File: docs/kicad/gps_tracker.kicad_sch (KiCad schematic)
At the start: 12 parts, among them J1 GNSS: Foxeer M10Q-250 / Beiti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, J2 BIGGA GSM (SIM800C) board, J3 SSD1306 0.96" OLED I2C 0x3C, J4 MicroSD SPI module, J5 Battery Shield V8, 2x18650, J6 BMA400 CJMCU-400 (not fitted 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, SW1 Button (BOOT-style, active lo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, U1 ESP32-S3-WROOM-1 (DevKitC-1)

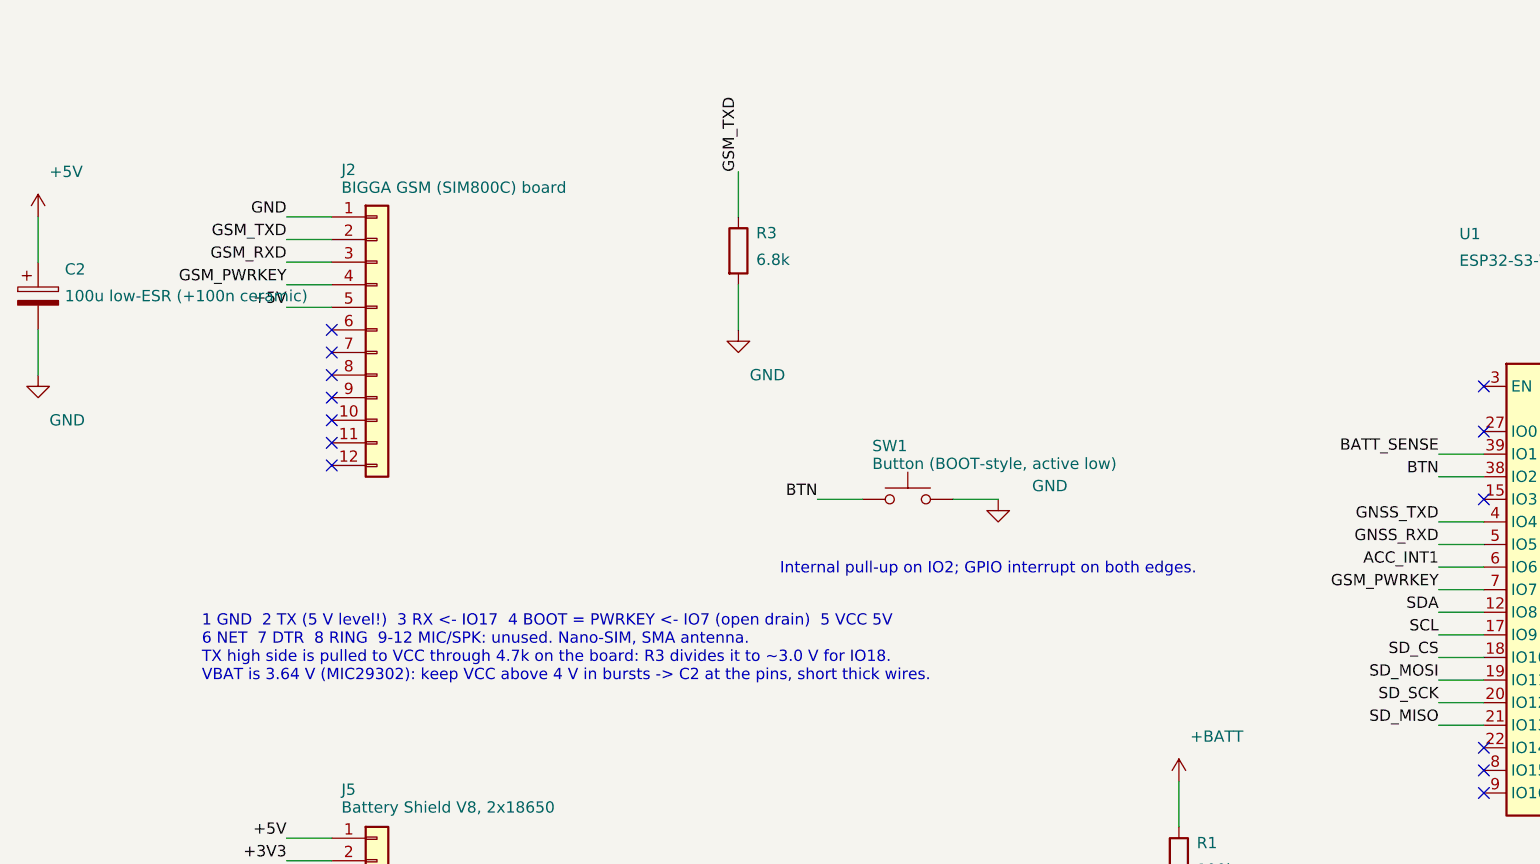
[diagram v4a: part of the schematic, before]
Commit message: Schematic: move C2 clear of the BIGGA header labels
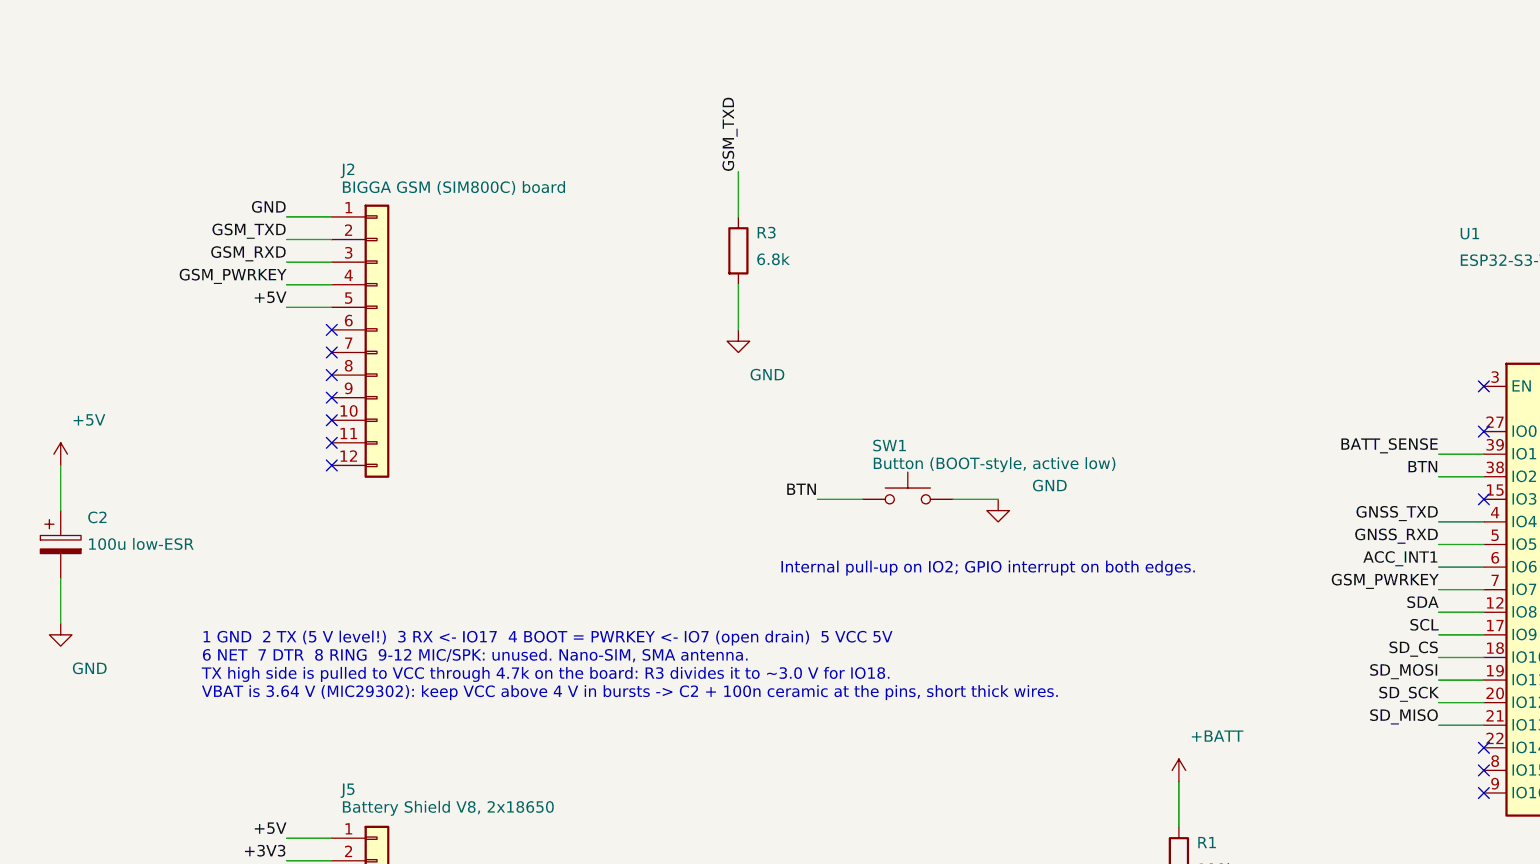
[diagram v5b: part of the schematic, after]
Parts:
- C2: value 100u low-ESR (+100n ceramic) -> 100u low-ESR
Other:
- note added: "1 GND 2 TX (5 V level!) 3 RX <- IO17 4 BOOT = PWRKEY <- IO7 (open drain) 5 VCC 5V 6 NET 7 DTR 8 RING 9-12 MIC/SPK: unused. Nano-SIM, SMA antenna. TX high side is pulled to VCC through 4.7k on the board: R3 divides it to ~3.0 V for IO18. VBAT is 3.64 V (MIC29302): keep VCC above 4 V in bursts -> C2 + 100n ceramic at the pins, short thick wires."
- note removed: "1 GND 2 TX (5 V level!) 3 RX <- IO17 4 BOOT = PWRKEY <- IO7 (open drain) 5 VCC 5V 6 NET 7 DTR 8 RING 9-12 MIC/SPK: unused. Nano-SIM, SMA antenna. TX high side is pulled to VCC through 4.7k on the board: R3 divides it to ~3.0 V for IO18. VBAT is 3.64 V (MIC29302): keep VCC above 4 V in bursts -> C2 at the pins, short thick wires."

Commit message: NET indicator LED on the BIGGA board: 1k + red LED on NETLIGHT
The modem's NETLIGHT output reaches the header as NET; blinking at 0.8 s
means searching, 3 s registered, 0.3 s GPRS transfer. A red LED through
1 k to GND makes that visible on the bench with no firmware involved and
no GPIO spent, which the SuperMini cannot spare. Added to the schematic
(R4, LED1), the hardware doc and the wiring sheet.
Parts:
- added LED1: red NET, symbol Device:LED
- added R4: 1k, symbol Device:R
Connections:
- net GND: now also LED1.1 (K)
- net GSM_NET: now reaches J2.6 (Pin_6)
- net GSM_NET: now also R4.1
- new net: LED1.2 (A), R4.2
- no-connect marks 31 -> 30
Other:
- note added: "1 GND 2 TX (5 V level!) 3 RX <- IO17 4 BOOT = PWRKEY <- IO7 (open drain) 5 VCC 5V 6 NET -> R4 1k -> LED1 (NETLIGHT: 0.8 s searching, 3 s registered, 0.3 s GPRS) 7 DTR 8 RING 9-12 audio: unused. TX high side is pulled to VCC through 4.7k on the board: R3 divides it to ~3.0 V for IO18. VBAT is 3.64 V (MIC29302): keep VCC above 4 V in bursts -> C2 + 100n ceramic at the pins, short thick wires."
- note removed: "1 GND 2 TX (5 V level!) 3 RX <- IO17 4 BOOT = PWRKEY <- IO7 (open drain) 5 VCC 5V 6 NET 7 DTR 8 RING 9-12 MIC/SPK: unused. Nano-SIM, SMA antenna. TX high side is pulled to VCC through 4.7k on the board: R3 divides it to ~3.0 V for IO18. VBAT is 3.64 V (MIC29302): keep VCC above 4 V in bursts -> C2 + 100n ceramic at the pins, short thick wires."

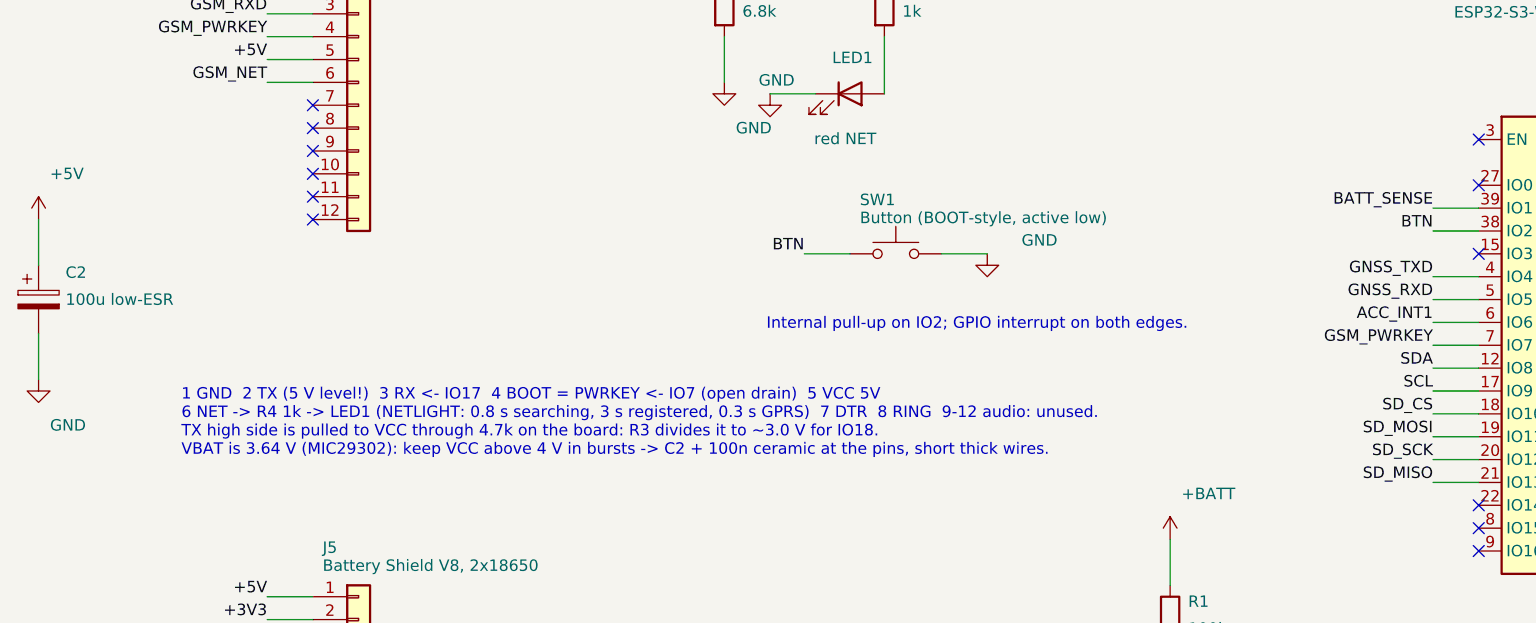
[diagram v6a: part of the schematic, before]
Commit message: BIGGA GSM: no external input capacitor, the board carries 100+10+1 uF at VCC
The board schematic shows C6/C5/C8 (100 uF, 10 uF, 1 uF) directly at the
VCC input, which is what the external 100 uF + ceramic was meant to
provide. Removed C2 from the schematic, the wiring diagram, the hardware
doc and the assembly sheet; short thick wires from the shield remain the
requirement, and the 1000 uF stays a brownout fallback only.
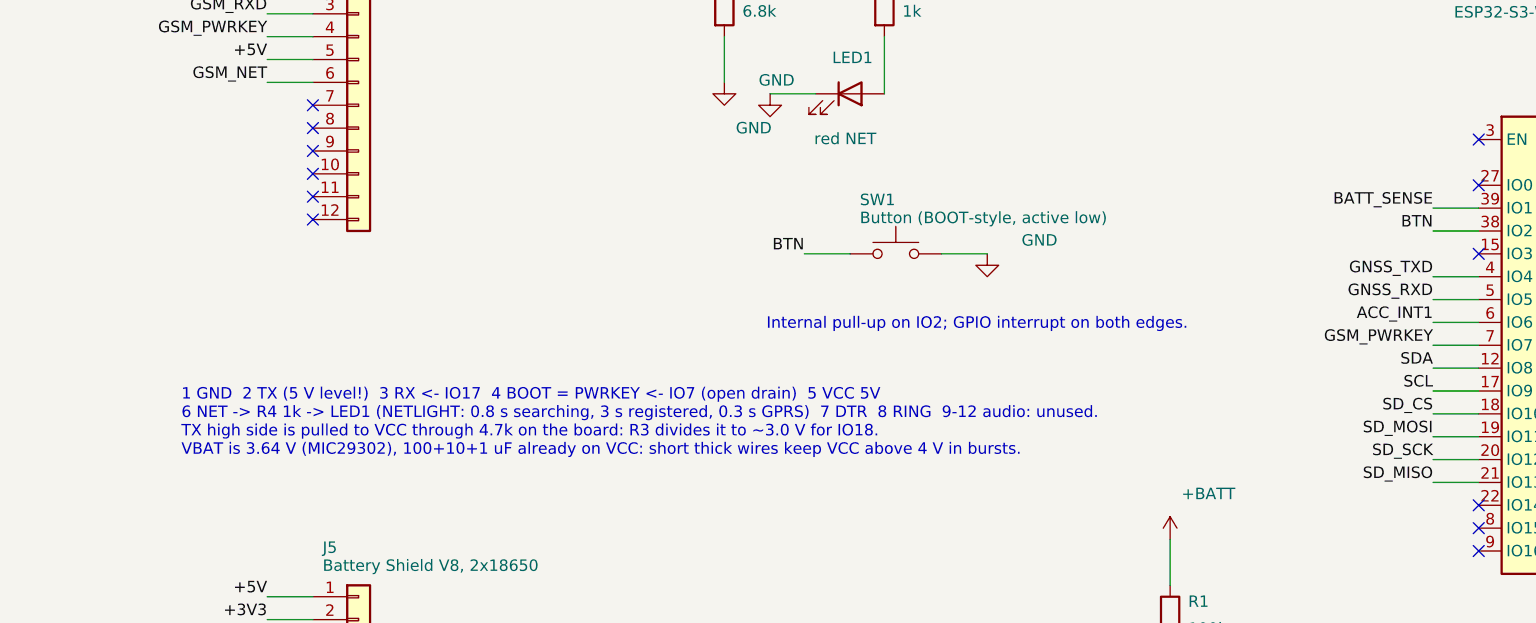
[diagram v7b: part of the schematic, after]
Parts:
- removed C2: 100u low-ESR, symbol Device:C_Polarized
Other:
- note added: "1 GND 2 TX (5 V level!) 3 RX <- IO17 4 BOOT = PWRKEY <- IO7 (open drain) 5 VCC 5V 6 NET -> R4 1k -> LED1 (NETLIGHT: 0.8 s searching, 3 s registered, 0.3 s GPRS) 7 DTR 8 RING 9-12 audio: unused. TX high side is pulled to VCC through 4.7k on the board: R3 divides it to ~3.0 V for IO18. VBAT is 3.64 V (MIC29302), 100+10+1 uF already on VCC: short thick wires keep VCC above 4 V in bursts."
- note removed: "1 GND 2 TX (5 V level!) 3 RX <- IO17 4 BOOT = PWRKEY <- IO7 (open drain) 5 VCC 5V 6 NET -> R4 1k -> LED1 (NETLIGHT: 0.8 s searching, 3 s registered, 0.3 s GPRS) 7 DTR 8 RING 9-12 audio: unused. TX high side is pulled to VCC through 4.7k on the board: R3 divides it to ~3.0 V for IO18. VBAT is 3.64 V (MIC29302): keep VCC above 4 V in bursts -> C2 + 100n ceramic at the pins, short thick wires."

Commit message: MicroSD: SCK on GPIO11, MOSI on GPIO12 for a straight header run
Swaps the two signals from SPI2's IOMUX pins (SCK 12, MOSI 11) so the card
module wires in order CS-SCK-MOSI-MISO on GPIO10-13. Through the GPIO
matrix the bus is limited to tens of MHz, far above the 10 MHz the card is
clocked at. Config, hardware doc, schematic, wiring diagram and README
updated; ERC clean.
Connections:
- net SD_MOSI: now also U1.20 (IO12); no longer U1.19 (IO11)
- net SD_SCK: now also U1.19 (IO11); no longer U1.20 (IO12)
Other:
- note added: "1 GND 2 VCC 3V3 (or 5V if the module has a level shifter) 3 MISO -> IO13 4 MOSI <- IO12 5 SCK <- IO11 6 CS <- IO10"
- note removed: "1 GND 2 VCC 3V3 (or 5V if the module has a level shifter) 3 MISO -> IO13 4 MOSI <- IO11 5 SCK <- IO12 6 CS <- IO10"
